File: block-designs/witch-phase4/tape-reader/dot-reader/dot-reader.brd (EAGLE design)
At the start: 73 x 45 mm, 24 parts, among them U1 QRE1113, U2 QRE1113, U3 QRE1113, U4 QRE1113, U5 QRE1113, U6 QRE1113

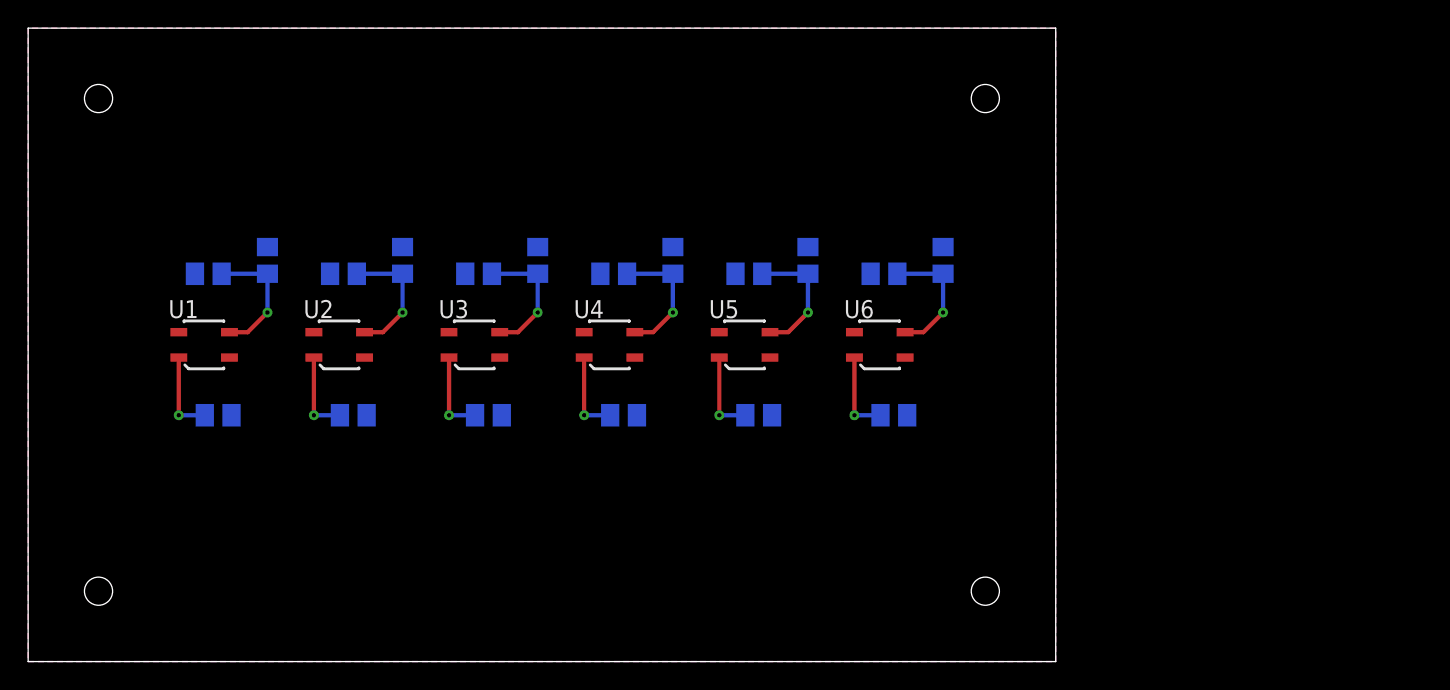
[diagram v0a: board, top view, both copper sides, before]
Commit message: first cut of a functional dot-reader pcb after changes to 80mm paper
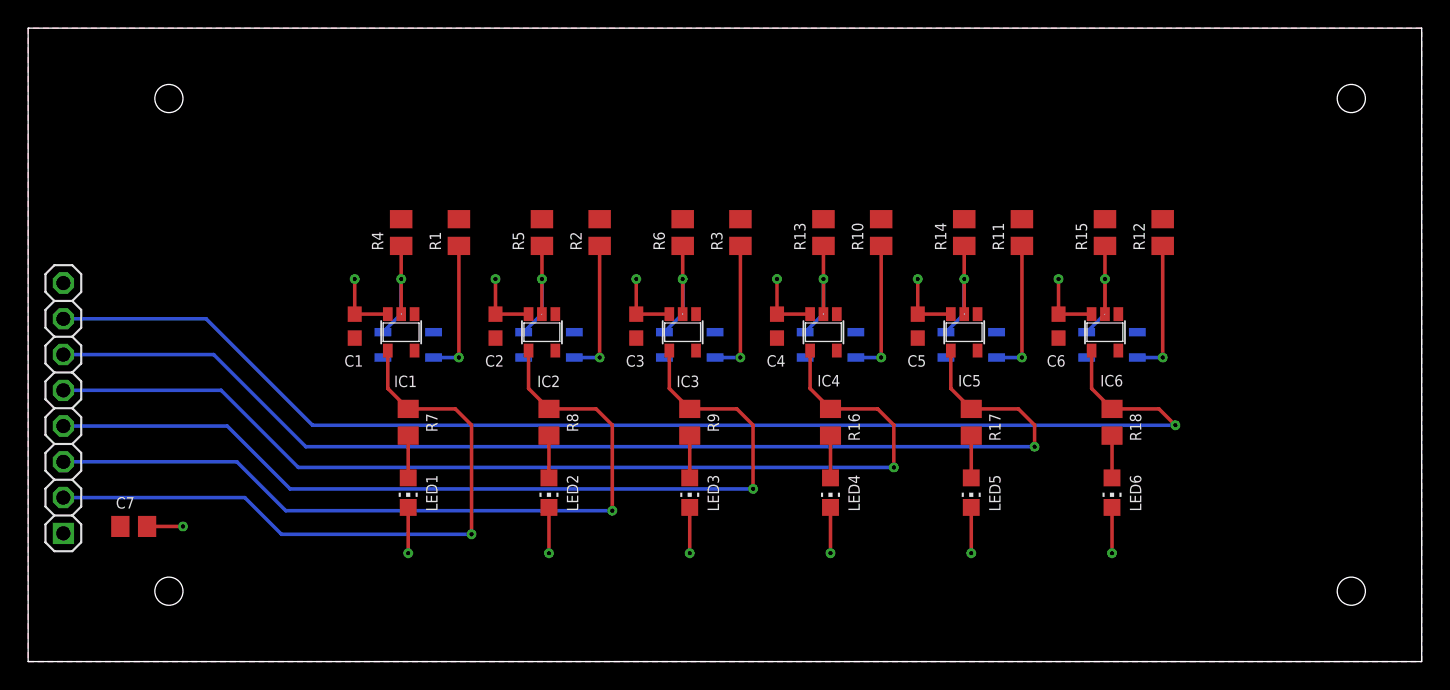
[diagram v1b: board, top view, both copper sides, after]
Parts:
- added C7: 10uF, resistor:C0805
- added IC1, IC2, IC3, IC4, IC5, IC6: 74LVC1G14DBV, 74xx-little-us:SOT23-5
- added JP1: (no value), custom-pinhead:1X08
- added LED1, LED2, LED3, LED4, LED5, LED6: (no value), led:CHIP-LED0805
- added R13, R14, R15: 10K, resistor:M0805
- added R16, R17, R18: 270, resistor:R0805
- C1, C2, C3, C4, C5, C6: value 10nF -> 0.1uF; device resistor:C0805 -> resistor:C0603
- R10, R12: value 220R -> 100R
- R2: value 200R -> 100R
- R4, R6: value 220R -> 10K
- R5: value 100R -> 10K
- R7, R9: value 100R -> 270; device resistor:M0805 -> resistor:R0805
- R8: value 220R -> 270; device resistor:M0805 -> resistor:R0805
- moved R3 30.4 mm to (50.6, 30.5), flipped to the top, turned to 90 degrees
- moved R2 28.0 mm to (40.6, 30.5), flipped to the top, turned to 90 degrees
- moved R1 21.5 mm to (30.6, 30.5), flipped to the top, turned to 90 degrees
- moved R12 20.0 mm to (80.6, 30.5), flipped to the top, turned to 90 degrees
- moved U6 16.5 mm to (77.0, 22.5), flipped to the bottom
- moved U5 16.1 mm to (67.0, 22.5), flipped to the bottom
- moved R11 15.9 mm to (70.6, 30.5), flipped to the top, turned to 90 degrees
- moved U4 15.7 mm to (57.0, 22.5), flipped to the bottom
- moved R7 15.3 mm to (27.0, 17.0), flipped to the top, turned to 270 degrees
- moved U3 15.3 mm to (47.0, 22.5), flipped to the bottom
- moved U2 14.9 mm to (37.0, 22.5), flipped to the bottom
- moved R6 14.8 mm to (46.5, 30.5), flipped to the top, turned to 90 degrees
- moved U1 14.5 mm to (27.0, 22.5), flipped to the bottom
- moved R5 13.5 mm to (36.5, 30.5), flipped to the top, turned to 90 degrees
- moved R8 11.5 mm to (37.0, 17.0), flipped to the top, turned to 270 degrees
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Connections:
- removed net N$12: C6.2, R12.2, U6.3
- new net !SENS_A: IC1.2, R4.1, U1.3
- new net !SENS_B: IC2.2, R5.1, U2.3
- new net !SENS_C: IC4.2, R13.1, U4.3
- new net !SENS_D: IC5.2, R14.1, U5.3
- new net !SENS_DOT: IC3.2, R6.1, U3.3
- new net !SENS_E: IC6.2, R15.1, U6.3
- new net N$20: LED1.A, R7.2
- net GND: now also C1.2, C2.2, C3.2, C4.2, C5.2, C6.2, C7.2, IC1.3, IC2.3, IC3.3, IC4.3, IC5.3, IC6.3, JP1.8, LED1.C, LED2.C, LED3.C, LED4.C, LED5.C, LED6.C
- net N$10: now also LED6.A, R18.2; no longer C5.2, R10.2, U5.3
- net N$11: now also R12.1; no longer R11.1
- net N$2: now also LED2.A, R8.2; no longer C1.2, R2.2, U1.3
- net N$3: now also R2.1; no longer R3.1
- net N$4: now also LED4.A, R16.2; no longer C2.2, R4.2, U2.3
- net N$5: now also R3.1; no longer R5.1
- net N$6: now also LED5.A, R17.2; no longer C3.2, R6.2, U3.3
- net N$7: now also R10.1; no longer R7.1
- net N$8: now also LED3.A, R9.2; no longer C4.2, R8.2, U4.3
- net N$9: now also R11.1; no longer R9.1
- net SENS_A: now also IC1.4, JP1.2, R7.1; no longer R2.1
- net SENS_B: now also IC2.4, JP1.3, R8.1; no longer R4.1
- net SENS_C: now also IC4.4, JP1.5, R16.1; no longer R8.1
- net SENS_D: now also IC5.4, JP1.6, R17.1; no longer R10.1
- net SENS_DOT: now also IC3.4, JP1.4, R9.1; no longer R6.1
- net SENS_E: now also IC6.4, JP1.7, R18.1; no longer R12.1
- net VCC: now also C7.1, IC1.5, IC2.5, IC3.5, IC4.5, IC5.5, IC6.5, JP1.1, R10.2, R12.2, R13.2, R14.2, R15.2, R2.2, R4.2, R6.2; no longer R7.2, R9.2
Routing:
- net SENS_E: track 0.00 -> 91.9 mm, vias 0 -> 1
- net SENS_D: track 0.00 -> 83.0 mm, vias 0 -> 1
- net SENS_C: track 0.00 -> 74.0 mm, vias 0 -> 1
- net SENS_DOT: track 0.00 -> 65.1 mm, vias 0 -> 1
- net SENS_B: track 0.00 -> 56.2 mm, vias 0 -> 1
- net GND: track 0.00 -> 51.1 mm, vias 0 -> 13
- net SENS_A: track 0.00 -> 47.6 mm, vias 0 -> 1
- net N$12: track 9.28 -> 0.00 mm, vias 1 -> 0
- net !SENS_A: track 0.00 -> 9.16 mm, vias 0 -> 1
- net !SENS_E: track 0.00 -> 9.16 mm, vias 0 -> 1
- net !SENS_DOT: track 0.00 -> 9.16 mm, vias 0 -> 1
- net !SENS_D: track 0.00 -> 9.16 mm, vias 0 -> 1
- net !SENS_C: track 0.00 -> 9.16 mm, vias 0 -> 1
- net !SENS_B: track 0.00 -> 9.16 mm, vias 0 -> 1
- net N$4: track 9.28 -> 3.00 mm, vias 1 -> 0
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- added copper zone on layer 16, net GND
- added copper zone on layer 1, net VCC
- removed copper zone on layer 1, net GND
- removed copper zone on layer 16, net VCC
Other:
- board size 73 x 45 mm -> 99 x 45 mm

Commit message: switch to non-inverting schmitts and layout cleanup
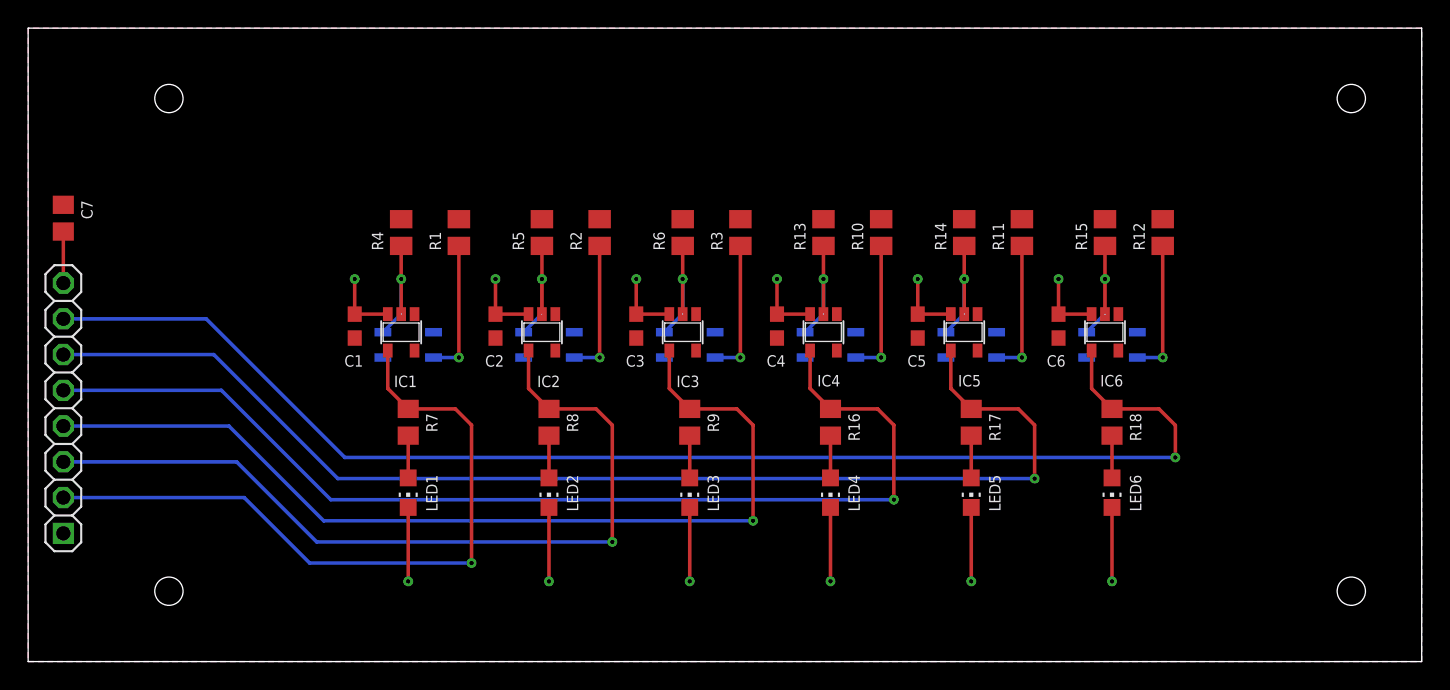
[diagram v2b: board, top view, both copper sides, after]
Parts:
- IC1, IC2, IC3, IC4, IC5, IC6: value 74LVC1G14DBV -> 74LVC1G17DBV
- moved C7 22.5 mm to (2.50, 31.5), turned to 270 degrees
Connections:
- net !SENS_A renamed A
- net !SENS_B renamed B
- net !SENS_C renamed C
- net !SENS_D renamed D
- net !SENS_DOT renamed DOT
- net !SENS_E renamed E
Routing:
- net GND: track 51.1 -> 64.2 mm, vias 13 -> 12
- net SENS_C: track 74.0 -> 77.2 mm
- net SENS_E: track 91.9 -> 95.1 mm
- net SENS_DOT: track 65.1 -> 68.3 mm
- net SENS_D: track 83.0 -> 86.2 mm
- net SENS_B: track 56.2 -> 59.4 mm
- net SENS_A: track 47.6 -> 50.5 mm
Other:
- board text added: "A"
- board text added: "B"
- board text added: "C"
- board text added: "D"
- board text added: "E"
- board text added: "VAL"

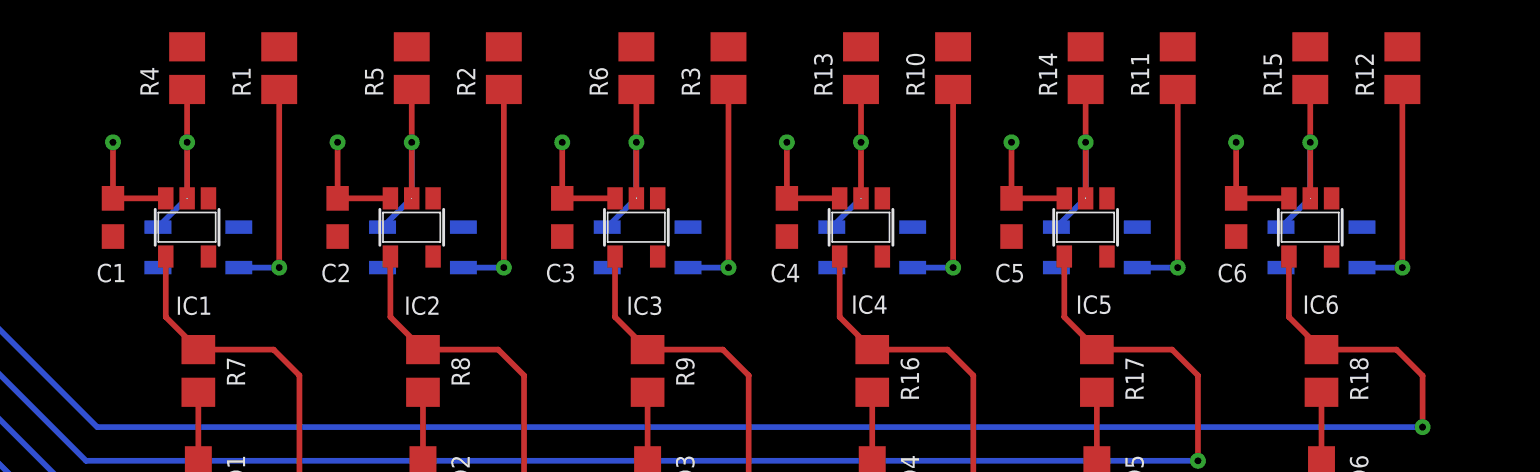
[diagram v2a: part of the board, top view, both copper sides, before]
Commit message: fix QRE1113 pcb footprint and reverse direction of signal labels
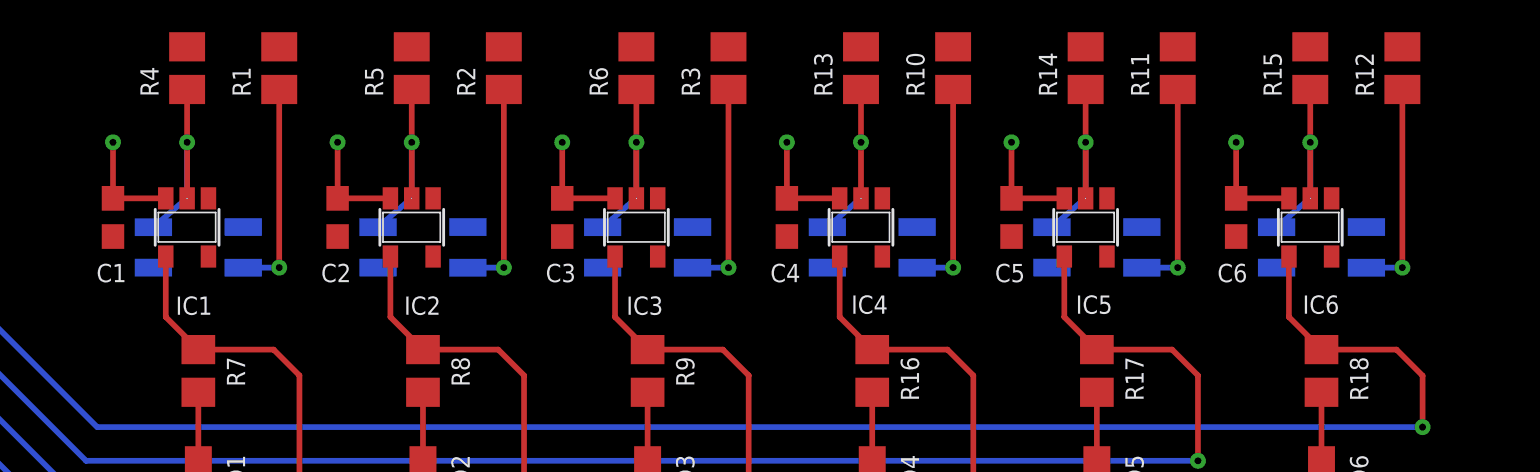
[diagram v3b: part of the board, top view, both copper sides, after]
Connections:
- net SENS_A renamed SENSE_E
- net SENS_B renamed SENSE_D
- net SENS_C renamed SENSE_DOT
- net SENS_D renamed SENSE_B
- net SENS_DOT renamed SENSE_C
- net SENS_E renamed SENSE_A
